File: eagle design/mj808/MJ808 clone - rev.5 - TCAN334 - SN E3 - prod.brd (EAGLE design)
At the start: 36.5 x 36.5 mm, 35 parts, among them IC202 LDK320AM33R, IC302 STM32F042G6U6, IC401 TCAN334, IC506 MAX16820, IC507 SQA470EEJ-T1_GE3, IC602 MAX6816EUS+T

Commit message: - created gerbers - sent to FAB
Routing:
- net 3V3: track 18.4 -> 17.7 mm
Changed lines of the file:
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@@
 <grid distance="0.25" unitdist="mm" unit="mm" style="lines" multiple="1" display="yes" altdistance="0.125" altunitdist="mm" altunit="mm"/>
 <layers>
-<layer number="1" name="Top" color="4" fill="1" visible="yes" active="yes"/>
-<layer number="2" name="Route2" color="1" fill="3" visible="no" active="yes"/>
+<layer number="1" name="Top" color="4" fill="1" visible="no" active="yes"/>
+<layer number="2" name="Route2" color="1" fill="3" visible="yes" active="yes"/>
 <layer number="3" name="Route3" color="4" fill="3" visible="no" active="no"/>
 <layer number="4" name="Route4" color="1" fill="4" visible="no" active="no"/>
@@
 <layer number="19" name="Unrouted" color="6" fill="1" visible="yes" active="yes"/>
 <layer number="20" name="Dimension" color="24" fill="1" visible="yes" active="yes"/>
-<layer number="21" name="tPlace" color="7" fill="1" visible="yes" active="yes"/>
+<layer number="21" name="tPlace" color="7" fill="1" visible="no" active="yes"/>
 <layer number="22" name="bPlace" color="7" fill="1" visible="no" active="yes"/>
-<layer number="23" name="tOrigins" color="15" fill="1" visible="yes" active="yes"/>
+<layer number="23" name="tOrigins" color="15" fill="1" visible="no" active="yes"/>
 <layer number="24" name="bOrigins" color="15" fill="1" visible="no" active="yes"/>
-<layer number="25" name="tNames" color="7" fill="1" visible="yes" active="yes"/>
+<layer number="25" name="tNames" color="7" fill="1" visible="no" active="yes"/>
 <layer number="26" name="bNames" color="7" fill="1" visible="no" active="yes"/>
 <layer number="27" name="tValues" color="7" fill="1" visible="no" active="yes"/>
 <layer number="28" name="bValues" color="7" fill="1" visible="no" active="yes"/>
-<layer number="29" name="tStop" color="7" fill="3" visible="yes" active="yes"/>
+<layer number="29" name="tStop" color="7" fill="3" visible="no" active="yes"/>
 <layer number="30" name="bStop" color="7" fill="6" visible="no" active="yes"/>
 <layer number="31" name="tCream" color="7" fill="4" visible="no" active="yes"/>
@@
 <layer number="37" name="tTest" color="7" fill="1" visible="no" active="yes"/>
 <layer number="38" name="bTest" color="7" fill="1" visible="no" active="yes"/>
-<layer number="39" name="tKeepout" color="4" fill="11" visible="yes" active="yes"/>
+<layer number="39" name="tKeepout" color="4" fill="11" visible="no" active="yes"/>
 <layer number="40" name="bKeepout" color="1" fill="11" visible="no" active="yes"/>
-<layer number="41" name="tRestrict" color="4" fill="10" visible="yes" active="yes"/>
+<layer number="41" name="tRestrict" color="4" fill="10" visible="no" active="yes"/>
 <layer number="42" name="bRestrict" color="1" fill="10" visible="no" active="yes"/>
 <layer number="43" name="vRestrict" color="2" fill="10" visible="yes" active="yes"/>
@@
 <layer number="49" name="Reference" color="7" fill="1" visible="no" active="yes"/>
 <layer number="50" name="dxf" color="7" fill="1" visible="no" active="no"/>
-<layer number="51" name="tDocu" color="7" fill="1" visible="yes" active="yes"/>
+<layer number="51" name="tDocu" color="7" fill="1" visible="no" active="yes"/>
 <layer number="52" name="bDocu" color="7" fill="1" visible="no" active="yes"/>
 <layer number="53" name="tGND_GNDA" color="7" fill="9" visible="no" active="no"/>
@@
 <text x="12.875" y="4.25" size="1" layer="22" font="vector" rot="MR0" align="center">GND</text>
 <text x="10.25" y="-3.75" size="1" layer="22" font="vector" rot="MR180" align="center">BAT+</text>
-<text x="-8" y="-1" size="0.75" layer="21" font="vector" align="center">H</text>
-<text x="-14" y="-1" size="0.75" layer="21" font="vector" align="center">L</text>
 <text x="-3.25" y="20.5" size="1.778" layer="1" font="vector" rot="R90">GND</text>
 <text x="0" y="20.5" size="1.778" layer="2" font="vector" rot="R90">3V3</text>
@@
 <text x="-20.5" y="3.25" size="1.778" layer="15" font="vector" rot="R180">GND</text>
 <text x="-20.5" y="4.5" size="1.778" layer="16" font="vector" rot="MR0">FRONT_LED_DRIVER:DIM_FRONT_DRAIN</text>
-<text x="-5" y="-13.75" size="0.75" layer="21" font="vector" rot="R180" align="center">LED
-and</text>
 <text x="-13" y="-33.5" size="1.778" layer="48">SuperNova E3 housing</text>
 <dimension x1="0" y1="18.25" x2="0" y2="-18.25" x3="-18.25" y3="0" textsize="1.778" layer="47"/>
@@
 <rectangle x1="-0.000128125" y1="0.244984375" x2="0.42659375" y2="0.2452375" layer="200"/>
 <rectangle x1="-0.000128125" y1="0.2452375" x2="0.42659375" y2="0.245490625" layer="200"/>
-<text x="4" y="-3.75" size="0.75" layer="21" font="vector" rot="R180" align="center">LED
-cat</text>
 <text x="-2.75" y="-12" size="1" layer="22" font="vector" rot="MR180" align="center">LED
 and</text>
@@
 <wire x1="8.25" y1="-3" x2="9" y2="-2" width="0.25" layer="22"/>
 <wire x1="9" y1="-2" x2="9.5" y2="-2" width="0.25" layer="22"/>
-<wire x1="10.5" y1="4.5" x2="11" y2="5" width="0.25" layer="22"/>
+<wire x1="10.25" y1="4.25" x2="11" y2="5" width="0.25" layer="22"/>
 <wire x1="12" y1="2" x2="13.5" y2="3.5" width="0.25" layer="22"/>
 </plain>
@@
 </element>
 <element name="IC302" library="STM32F042G6" package="UFQFPN-28" value="STM32F042G6U6" x="-4.75" y="9.5" smashed="yes">
-<attribute name="NAME" x="-7.5" y="9.5" size="0.5" layer="25" font="vector" rot="R270" align="center"/>
+<attribute name="NAME" x="-7.75" y="9.5" size="0.5" layer="25" font="vector" rot="R90" align="center"/>
 <attribute name="VALUE" x="-4.75" y="6.75" size="0.5" layer="27" font="vector" align="center"/>
 </element>
@@
 </element>
 <element name="C304" library="rcl" library_urn="urn:adsk.eagle:library:334" package="C0402" package3d_urn="urn:adsk.eagle:package:23626/2" value="1uF / 10V" x="-9.25" y="7.5" smashed="yes" rot="R90">
-<attribute name="NAME" x="-8.25" y="7.5" size="0.5" layer="25" font="vector" rot="R270" align="center"/>
+<attribute name="NAME" x="-10.25" y="7.5" size="0.5" layer="25" font="vector" rot="R270" align="center"/>
 <attribute name="POPULARITY" value="18" x="-9.25" y="7.5" size="1.778" layer="27" rot="R90" display="off"/>
 <attribute name="SPICEPREFIX" value="C" x="-9.25" y="7.5" size="1.778" layer="27" rot="R90" display="off"/>
@@
 </element>
 <element name="C307" library="rcl" library_urn="urn:adsk.eagle:library:334" package="C0402" package3d_urn="urn:adsk.eagle:package:23626/2" value="0.1uF / 10V" x="-9.25" y="11" smashed="yes" rot="R270">
-<attribute name="NAME" x="-8.25" y="11" size="0.5" layer="25" font="vector" rot="R90" align="center"/>
+<attribute name="NAME" x="-10.25" y="11" size="0.5" layer="25" font="vector" rot="R90" align="center"/>
 <attribute name="POPULARITY" value="18" x="-9.25" y="11" size="1.778" layer="27" rot="R270" display="off"/>
 <attribute name="SPICEPREFIX" value="C" x="-9.25" y="11" size="1.778" layer="27" rot="R270" display="off"/>
@@
 <wire x1="0.6" y1="8.15" x2="0.75" y2="8" width="0.25" layer="1"/>
 <via x="0.75" y="8" extent="1-16" drill="0.35"/>
-<wire x1="-9.25" y1="8.15" x2="-9.35" y2="8.25" width="0.25" layer="1"/>
-<wire x1="-9.35" y1="8.25" x2="-10.25" y2="8.25" width="0.25" layer="1"/>
-<via x="-10.25" y="8.25" extent="1-16" drill="0.35"/>
+<wire x1="-9.25" y1="8.15" x2="-9.25" y2="8.5" width="0.25" layer="1"/>
+<via x="-9.25" y="8.5" extent="1-16" drill="0.35"/>
 <wire x1="14" y1="2.5" x2="13.992" y2="2.492" width="0.25" layer="1"/>
 <wire x1="13.992" y1="2.492" x2="13.4" y2="2.492" width="0.25" layer="1"/>

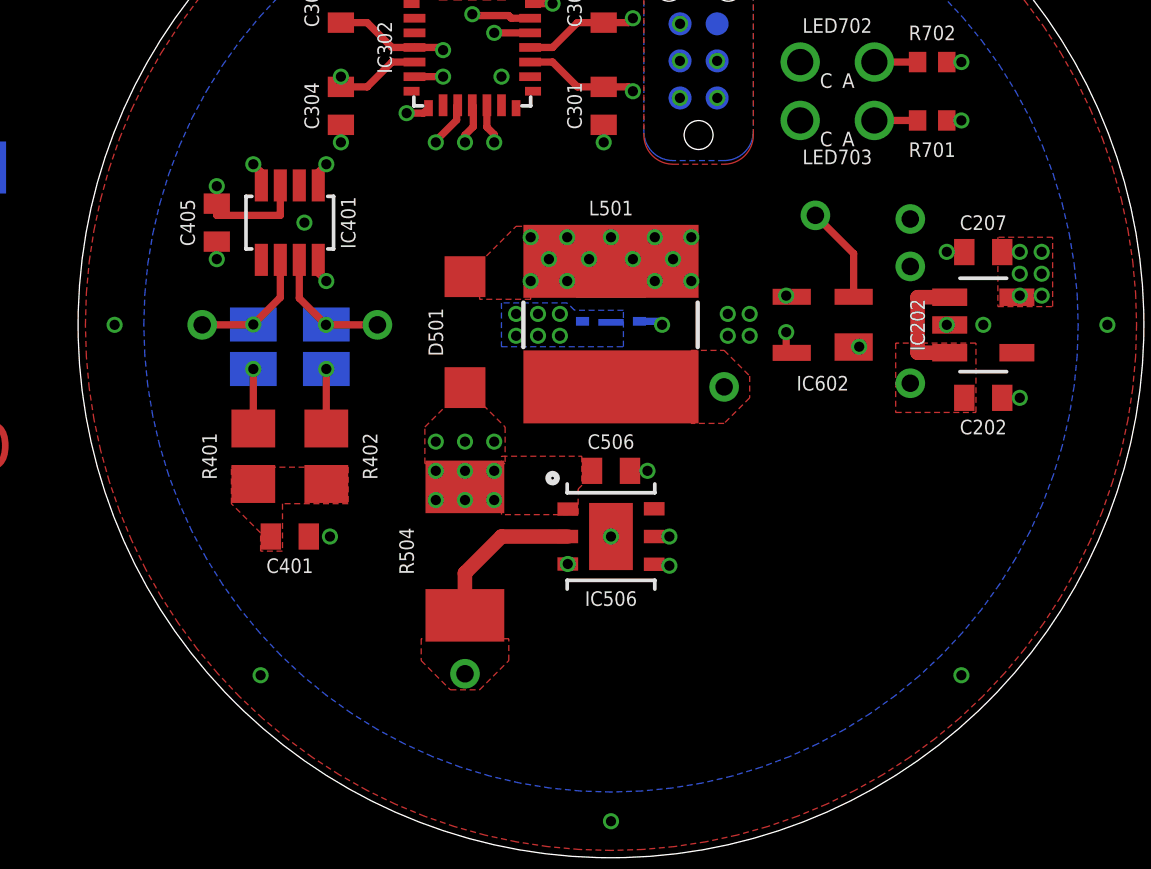
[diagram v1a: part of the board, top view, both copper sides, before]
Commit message: in mj808/mj818 brds: - resized TH drills for wire connections from 0.6 to 0.9mm
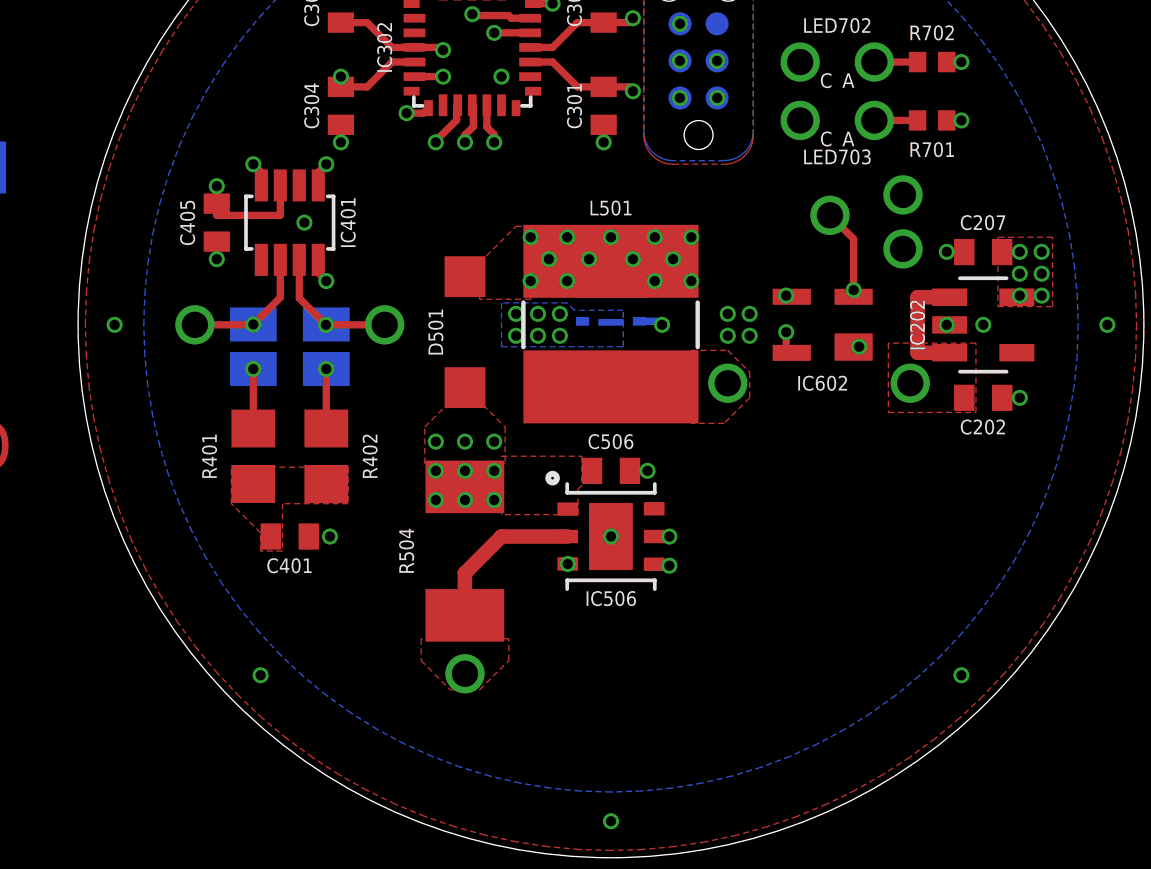
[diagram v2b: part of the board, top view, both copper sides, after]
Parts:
- TP1, TP2, TP3, TP4, TP5, TP6, TP601, TP602: device signal testpoint:TH-0.6 -> signal testpoint:TH-0.9
- moved TP602 0.86 mm to (10.0, 4.45)
- moved TP2 0.65 mm to (10.0, 2.60), turned to 180 degrees
- moved TP601 0.50 mm to (7.50, 3.75)
- moved TP5 0.25 mm to (-7.75, 0.00)
- moved TP6 0.25 mm to (-14.2, 0.00)
- moved TP4 0.18 mm to (4.00, -2.00)
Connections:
- net BAT+: now also TP1.P$1; no longer TP1.TP$1
- net CAN_H: now also TP5.P$1; no longer TP5.TP$1
- net CAN_L: now also TP6.P$1; no longer TP6.TP$1
- net GND: now also TP2.P$1, TP602.P$1; no longer TP2.TP$1, TP602.TP$1
- net LED_AN: now also TP3.P$1; no longer TP3.TP$1
- net LED_CA: now also TP4.P$1; no longer TP4.TP$1
- net PUSHBUTTON:SWITCH_IN: now also TP601.P$1; no longer TP601.TP$1
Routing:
- net PUSHBUTTON:SWITCH_IN: track 3.33 -> 3.13 mm, vias 0 -> 1

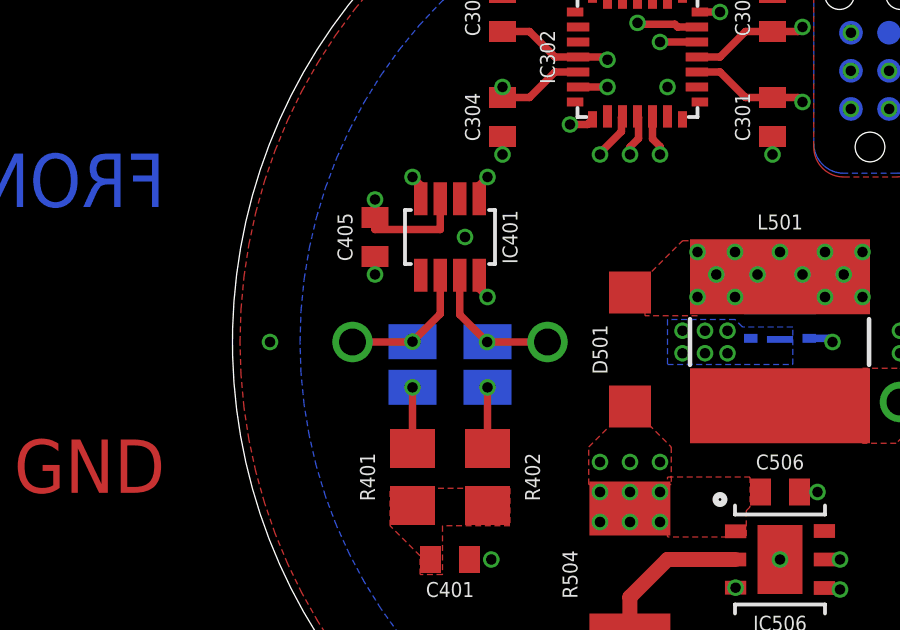
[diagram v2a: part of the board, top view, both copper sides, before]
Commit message: in mj808 & mj818 design: - added 2nd TH via for CAN H & L connection
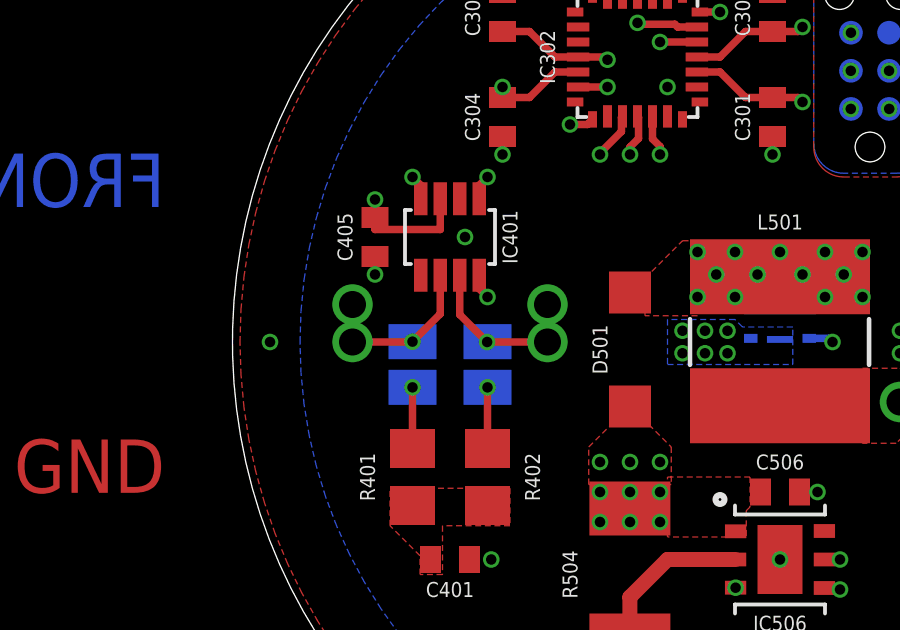
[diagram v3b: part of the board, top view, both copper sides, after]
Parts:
- added TP7: CAN high, signal testpoint:TH-0.9
- added TP8: CAN low, signal testpoint:TH-0.9
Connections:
- net CAN_H: now also TP7.P$1
- net CAN_L: now also TP8.P$1
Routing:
- net CAN_L: track 4.60 -> 5.85 mm
- net CAN_H: track 4.63 -> 5.88 mm
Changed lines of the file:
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@@
 <grid distance="0.25" unitdist="mm" unit="mm" style="lines" multiple="1" display="yes" altdistance="0.125" altunitdist="mm" altunit="mm"/>
 <layers>
-<layer number="1" name="Top" color="4" fill="1" visible="yes" active="yes"/>
-<layer number="2" name="Route2" color="1" fill="3" visible="no" active="yes"/>
+<layer number="1" name="Top" color="4" fill="1" visible="no" active="yes"/>
+<layer number="2" name="Route2" color="1" fill="3" visible="yes" active="yes"/>
 <layer number="3" name="Route3" color="4" fill="3" visible="no" active="no"/>
 <layer number="4" name="Route4" color="1" fill="4" visible="no" active="no"/>
@@
 <layer number="19" name="Unrouted" color="6" fill="1" visible="yes" active="yes"/>
 <layer number="20" name="Dimension" color="24" fill="1" visible="yes" active="yes"/>
-<layer number="21" name="tPlace" color="7" fill="1" visible="yes" active="yes"/>
+<layer number="21" name="tPlace" color="7" fill="1" visible="no" active="yes"/>
 <layer number="22" name="bPlace" color="7" fill="1" visible="no" active="yes"/>
-<layer number="23" name="tOrigins" color="15" fill="1" visible="yes" active="yes"/>
+<layer number="23" name="tOrigins" color="15" fill="1" visible="no" active="yes"/>
 <layer number="24" name="bOrigins" color="15" fill="1" visible="no" active="yes"/>
-<layer number="25" name="tNames" color="7" fill="1" visible="yes" active="yes"/>
+<layer number="25" name="tNames" color="7" fill="1" visible="no" active="yes"/>
 <layer number="26" name="bNames" color="7" fill="1" visible="no" active="yes"/>
 <layer number="27" name="tValues" color="7" fill="1" visible="no" active="yes"/>
 <layer number="28" name="bValues" color="7" fill="1" visible="no" active="yes"/>
-<layer number="29" name="tStop" color="7" fill="3" visible="yes" active="yes"/>
+<layer number="29" name="tStop" color="7" fill="3" visible="no" active="yes"/>
 <layer number="30" name="bStop" color="7" fill="6" visible="no" active="yes"/>
 <layer number="31" name="tCream" color="7" fill="4" visible="no" active="yes"/>
@@
 <layer number="37" name="tTest" color="7" fill="1" visible="no" active="yes"/>
 <layer number="38" name="bTest" color="7" fill="1" visible="no" active="yes"/>
-<layer number="39" name="tKeepout" color="4" fill="11" visible="yes" active="yes"/>
+<layer number="39" name="tKeepout" color="4" fill="11" visible="no" active="yes"/>
 <layer number="40" name="bKeepout" color="1" fill="11" visible="no" active="yes"/>
-<layer number="41" name="tRestrict" color="4" fill="10" visible="yes" active="yes"/>
+<layer number="41" name="tRestrict" color="4" fill="10" visible="no" active="yes"/>
 <layer number="42" name="bRestrict" color="1" fill="10" visible="no" active="yes"/>
 <layer number="43" name="vRestrict" color="2" fill="10" visible="yes" active="yes"/>
@@
 <layer number="49" name="Reference" color="7" fill="1" visible="no" active="yes"/>
 <layer number="50" name="dxf" color="7" fill="1" visible="no" active="no"/>
-<layer number="51" name="tDocu" color="7" fill="1" visible="yes" active="yes"/>
+<layer number="51" name="tDocu" color="7" fill="1" visible="no" active="yes"/>
 <layer number="52" name="bDocu" color="7" fill="1" visible="no" active="yes"/>
 <layer number="53" name="tGND_GNDA" color="7" fill="9" visible="no" active="no"/>
@@
 <attribute name="VALUE" x="11.635" y="8.905" size="1.27" layer="27" rot="R180"/>
 </element>
+<element name="TP7" library="signal testpoint" package="TH-0.9" value="CAN high" x="-7.75" y="1.25" smashed="yes" rot="MR0"/>
+<element name="TP8" library="signal testpoint" package="TH-0.9" value="CAN low" x="-14.25" y="1.25" smashed="yes" rot="MR0"/>
 </elements>
 <signals>
@@
 <via x="-9.762" y="0" extent="1-16" drill="0.35"/>
 <wire x1="-7.75" y1="0" x2="-9.762" y2="0" width="0.25" layer="1"/>
+<contactref element="TP7" pad="P$1"/>
+<wire x1="-7.75" y1="1.25" x2="-7.75" y2="0" width="0.25" layer="1"/>
 </signal>
 <signal name="CAN_L" class="3">
@@
 <wire x1="-14.25" y1="0" x2="-12.262" y2="0" width="0.25" layer="1"/>
 <wire x1="-12.262" y1="0" x2="-12.25" y2="0.012" width="0.25" layer="1"/>
+<contactref element="TP8" pad="P$1"/>
+<wire x1="-14.25" y1="1.25" x2="-14.25" y2="0" width="0.25" layer="1"/>
 </signal>
 <signal name="3V3" class="4">
@@
 <wire x1="-4.715" y1="6.785" x2="-5" y2="6.5" width="0.25" layer="1"/>
 <via x="-9.75" y="1.5" extent="1-16" drill="0.35"/>
-<wire x1="-5" y1="6.25" x2="-5" y2="5.25" width="0.25" layer="2"/>
-<wire x1="-5" y1="5.25" x2="-8.75" y2="1.5" width="0.25" layer="2"/>
-<wire x1="-8.75" y1="1.5" x2="-9.75" y2="1.5" width="0.25" layer="2"/>
+<wire x1="-5" y1="6.25" x2="-5" y2="5.5" width="0.25" layer="2"/>
+<wire x1="-5" y1="5.5" x2="-6.5" y2="4" width="0.25" layer="2"/>
+<wire x1="-6.5" y1="4" x2="-7.75" y2="4" width="0.25" layer="2"/>
+<wire x1="-7.75" y1="4" x2="-9.75" y2="2" width="0.25" layer="2"/>
+<wire x1="-9.75" y1="2" x2="-9.75" y2="1.5" width="0.25" layer="2"/>
 <wire x1="-10.025" y1="2.225" x2="-10.025" y2="1.775" width="0.25" layer="1"/>
 <wire x1="-9.75" y1="1.5" x2="-10.025" y2="1.775" width="0.25" layer="1"/>
